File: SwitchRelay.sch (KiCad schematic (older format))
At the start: 12 parts, among them J1 Decoder, J2 Switch, J3 Point, J4 AUX, K1 HFD2_xxx-x-L2

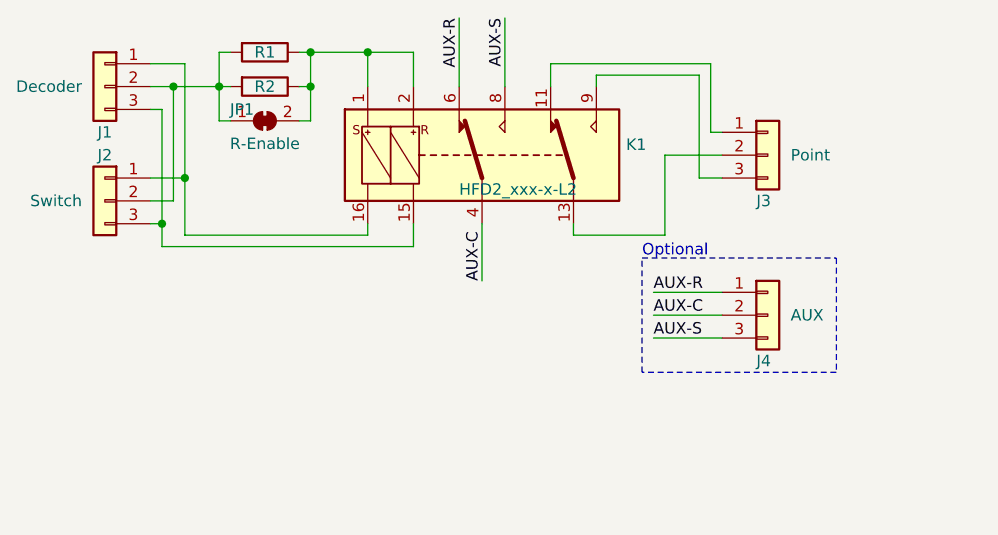
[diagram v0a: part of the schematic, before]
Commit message: Made version 2 with RT314F24
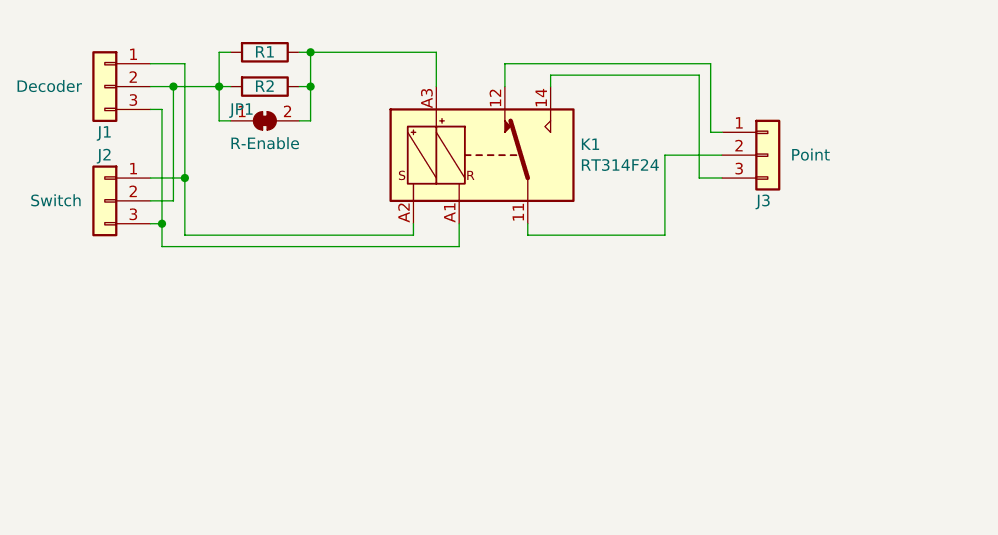
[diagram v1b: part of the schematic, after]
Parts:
- removed J4: AUX, TerminalBlock:TerminalBlock_bornier-3_P5.08mm, symbol Connector_Generic:Conn_01x03
- removed K1: HFD2_xxx-x-L2, septillion_relay:HFD2_xxx-x-L2, symbol septillion_relay:HFD2_xxx-x-L2
- added K1: RT314F24, septillion_relay:RTxxxFxx, symbol septillion_relay:RT314F12
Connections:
- net at JP1.2 (B), R1.1, R2.1: now also K1.A3
- net at J3.1 (Pin_1): now also K1.12
- net at J3.2 (Pin_2): now also K1.11
- net at J1.3 (Pin_3), J2.3 (Pin_3): now also K1.A1
- net at J1.1 (Pin_1), J2.1 (Pin_1): now also K1.A2
- net at J3.3 (Pin_3): now also K1.14
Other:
- note removed: "Optional"
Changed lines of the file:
@@
 	6750 3600 6750 3950
-Wire Wire Line
-	6750 3950 6350 3950
-Wire Wire Line
-	6350 3950 6350 3900
-Wire Wire Line
-	6450 3300 6450 3250
-Wire Wire Line
-	6450 3250 6900 3250
 Wire Wire Line
 	6900 3250 6900 3700
@@
 Wire Wire Line
 	6950 3500 6950 3200
-Wire Wire Line
-	6950 3200 6250 3200
-Wire Wire Line
-	6250 3200 6250 3300
-Text Label 5950 4150 1    50   ~ 0
-AUX-C
-Wire Wire Line
-	5950 4150 5950 3900
-Text Label 5850 3000 3    50   ~ 0
-AUX-R
-Text Label 6050 3000 3    50   ~ 0
-AUX-S
-Wire Wire Line
-	6050 3000 6050 3300
-Wire Wire Line
-	5850 3300 5850 3000
-$Comp
-L Connector_Generic:Conn_01x03 J4
-U 1 1 5D6A54C3
-P 7200 4300
-F 0 "J4" H 7150 4100 50  0000 L CNN
-F 1 "AUX" H 7300 4300 50  0000 L CNN
-F 2 "TerminalBlock:TerminalBlock_bornier-3_P5.08mm" H 7200 4300 50  0001 C CNN
-F 3 "~" H 7200 4300 50  0001 C CNN
-	1    7200 4300
-	1    0    0    -1
-$EndComp
-Text Label 6700 4300 0    50   ~ 0
-AUX-C
-Text Label 6700 4200 0    50   ~ 0
-AUX-R
-Text Label 6700 4400 0    50   ~ 0
-AUX-S
-Wire Wire Line
-	6700 4200 7000 4200
-Wire Wire Line
-	7000 4300 6700 4300
-Wire Wire Line
-	6700 4400 7000 4400
 $Comp
 L Device:R R1
@@
 	1    0    0    -1
 $EndComp
-Wire Notes Line
-	7500 4050 7500 4550
-Wire Notes Line
-	7500 4550 6650 4550
-Wire Notes Line
-	6650 4550 6650 4050
-Wire Notes Line
-	6650 4050 7500 4050
-Text Notes 6650 4050 0    50   ~ 0
-Optional
-$Comp
-L septillion_relay:HFD2_xxx-x-L2 K1
-U 1 1 5D69AF73
-P 5950 3600
-F 0 "K1" H 6580 3646 50  0000 L CNN
-F 1 "HFD2_xxx-x-L2" H 5850 3450 50  0000 L CNN
-F 2 "septillion_relay:HFD2_xxx-x-L2" H 6500 3650 50  0001 C CNN
-F 3 "http://www.hongfa.com:8080/pdfjs/web/viewer.html?file=/Uploads/PDF/HFD2_en.pdf" H 5750 3600 50  0001 C CNN
-	1    5950 3600
-	1    0    0    -1
-$EndComp
 Wire Wire Line
-	5450 3300 5450 3150
-Wire Wire Line
-	5450 3150 5650 3150
-Wire Wire Line
-	5650 3150 5650 3300
-Wire Wire Line
-	5200 3150 5450 3150
+	5750 3150 5750 3300
 Connection ~ 5200 3150
-Connection ~ 5450 3150
 Wire Wire Line
 	4650 3700 4650 3950
-Wire Wire Line
-	4650 3950 5450 3950
-Wire Wire Line
-	5450 3950 5450 3900
-Wire Wire Line
-	5650 4000 5650 3900
-Wire Wire Line
-	4550 4000 5650 4000
 Wire Wire Line
 	4550 3400 4500 3400
@@
 Wire Wire Line
 	4800 3300 4800 3150
+Wire Wire Line
+	5200 3150 5750 3150
+Wire Wire Line
+	5850 4000 5850 3900
+Wire Wire Line
+	4550 4000 5850 4000
+Wire Wire Line
+	5650 3950 5650 3900
+Wire Wire Line
+	4650 3950 5650 3950
+Wire Wire Line
+	6050 3200 6050 3300
+Wire Wire Line
+	6050 3200 6950 3200
+Wire Wire Line
+	6250 3300 6250 3250
+Wire Wire Line
+	6250 3250 6900 3250
+Wire Wire Line
+	6150 3900 6150 3950
+Wire Wire Line
+	6150 3950 6750 3950
+$Comp
+L septillion_relay:RT314F12 K1
+U 1 1 5D6E170A
+P 5950 3600
+F 0 "K1" H 6380 3646 50  0000 L CNN
+F 1 "RT314F24" H 6380 3555 50  0000 L CNN
+F 2 "septillion_relay:RTxxxFxx" H 6500 3650 50  0001 C CNN
+F 3 "https://www.te.com/commerce/DocumentDelivery/DDEController?Action=srchrtrv&DocNm=RT1_bistable&DocType=DS&DocLang=English" H 5950 3600 50  0001 C CNN
+	1    5950 3600
+	1    0    0    -1
+$EndComp
 $EndSCHEMATC

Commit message: Small changes
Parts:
- K1: value RT314F24 -> RT314Fxx
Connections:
- net at J1.1 (Pin_1), J2.1 (Pin_1): now also K1.A1; no longer K1.A2
- net at J1.3 (Pin_3), J2.3 (Pin_3): now also K1.A2; no longer K1.A1
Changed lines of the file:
@@
 	5200 3150 5750 3150
-Wire Wire Line
-	5850 4000 5850 3900
-Wire Wire Line
-	4550 4000 5850 4000
-Wire Wire Line
-	5650 3950 5650 3900
-Wire Wire Line
-	4650 3950 5650 3950
 Wire Wire Line
 	6050 3200 6050 3300
@@
 P 5950 3600
 F 0 "K1" H 6380 3646 50  0000 L CNN
-F 1 "RT314F24" H 6380 3555 50  0000 L CNN
+F 1 "RT314Fxx" H 6380 3555 50  0000 L CNN
 F 2 "septillion_relay:RTxxxFxx" H 6500 3650 50  0001 C CNN
 F 3 "https://www.te.com/commerce/DocumentDelivery/DDEController?Action=srchrtrv&DocNm=RT1_bistable&DocType=DS&DocLang=English" H 5950 3600 50  0001 C CNN
@@
 	1    0    0    -1
 $EndComp
+Wire Wire Line
+	4650 3950 5850 3950
+Wire Wire Line
+	5850 3950 5850 3900
+Wire Wire Line
+	5650 3900 5650 4000
+Wire Wire Line
+	5650 4000 4550 4000
 $EndSCHEMATC
